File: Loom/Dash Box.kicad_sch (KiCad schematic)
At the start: 28 parts, among them J10 VCU CAN, J11 VCU INPUTS, J12 DASH, J13 OUTPUTS, J14 RTDS, J60 Datalogger Connector, J63 CAN, J64 PWR, J65 MCU_DIN, J66 Segment Display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

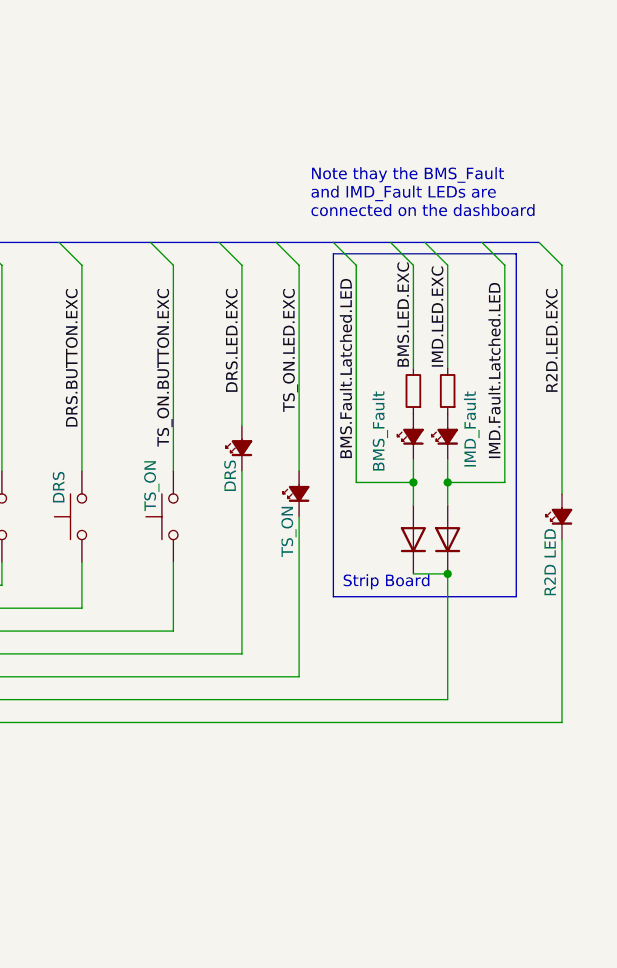
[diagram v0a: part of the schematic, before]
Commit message: fix(Loom): made requested changes + chores
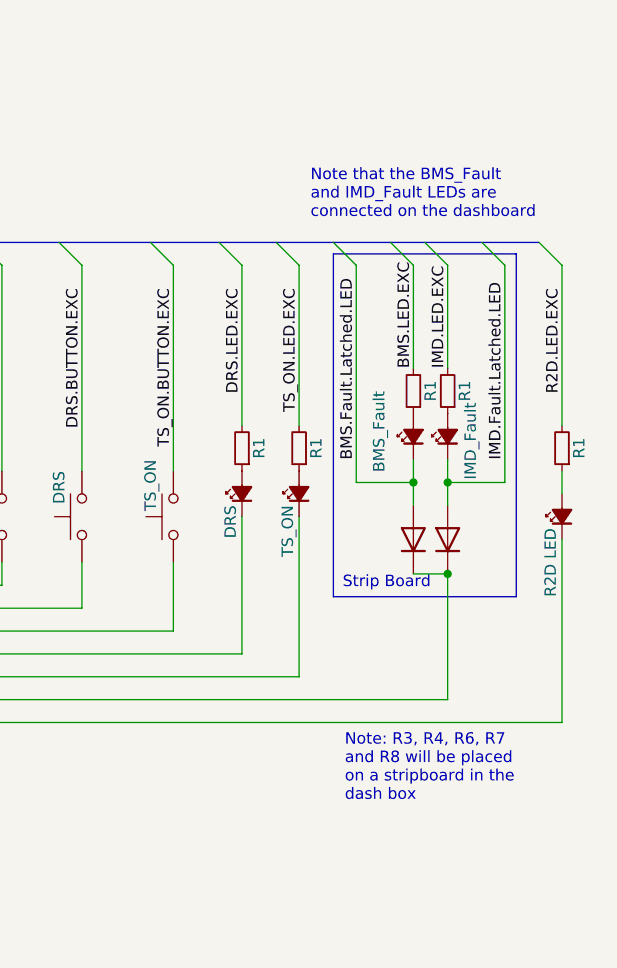
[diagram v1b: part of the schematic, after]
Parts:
- added R1 (x3): R_Small, symbol Device:R_Small
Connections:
- net BMS.LED.EXC: now also R1.2, R1.2, R1.2; no longer D1.2 (A), D2.2 (A), D4.2 (A)
- new net: D4.2 (A), R1.1
- new net: D1.2 (A), R1.1
- new net: D2.2 (A), R1.1
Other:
- note added: "Note that the BMS_Fault and IMD_Fault LEDs are connected on the dashboard"
- note added: "Note: R3, R4, R6, R7 and R8 will be placed on a stripboard in the dash box"
- note removed: "Note thay the BMS_Fault and IMD_Fault LEDs are connected on the dashboard"
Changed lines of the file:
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@@
     (stroke (width 0) (type default))
   )
-  (wire (pts (xy 246.38 68.58) (xy 246.38 88.9))
+  (wire (pts (xy 246.38 73.66) (xy 246.38 88.9))
     (stroke (width 0) (type default))
   )
@@
     (stroke (width 0) (type default))
   )
-  (wire (pts (xy 252.73 45.72) (xy 252.73 68.58))
+  (wire (pts (xy 252.73 45.72) (xy 252.73 63.5))
     (stroke (width 0) (type default))
   )
@@
     (stroke (width 0) (type default))
   )
+  (wire (pts (xy 281.94 68.58) (xy 281.94 71.12))
+    (stroke (width 0) (type default))
+  )
   (wire (pts (xy 78.74 63.5) (xy 101.6 63.5))
     (stroke (width 0) (type default))
@@
     (stroke (width 0) (type default))
   )
-  (wire (pts (xy 281.94 45.72) (xy 281.94 71.12))
+  (wire (pts (xy 281.94 45.72) (xy 281.94 63.5))
     (stroke (width 0) (type default))
   )
@@
     (effects (font (size 1.27 1.27) (color 72 72 72 1)) (justify top))
   )
-  (text "Note thay the BMS_Fault \nand IMD_Fault LEDs are \nconnected on the dashboard"
+  (text "Note: R3, R4, R6, R7\nand R8 will be placed\non a stripboard in the\ndash box"
+    (at 257.81 105.41 0)
+    (effects (font (size 1.27 1.27) (color 255 0 255 1)) (justify left bottom))
+  )
+  (text "Note that the BMS_Fault \nand IMD_Fault LEDs are \nconnected on the dashboard"
     (at 254 40.64 0)
     (effects (font (size 1.27 1.27) (color 255 0 255 1)) (justify left bottom))
@@
     (effects (font (size 1.27 1.27)) (justify left bottom))
   )
-  (label "IMD.LED.EXC" (at 101.6 63.5 180)
-    (effects (font (size 1.27 1.27)) (justify right bottom))
-  )
-  (label "BMS.Fault.Latched.LED" (at 259.08 67.31 90)
+  (label "IMD.LED.EXC" (at 101.6 63.5 180) (fields_autoplaced)
+    (effects (font (size 1.27 1.27)) (justify right bottom))
+  )
+  (label "BMS.Fault.Latched.LED" (at 259.08 67.31 90) (fields_autoplaced)
     (effects (font (size 1.27 1.27)) (justify left bottom))
   )
@@
     (effects (font (size 1.27 1.27)) (justify left bottom))
   )
-  (label "WSS.SIG" (at 139.7 25.4 270)
+  (label "WSS.SIG" (at 139.7 25.4 270) (fields_autoplaced)
     (effects (font (size 1.27 1.27)) (justify right bottom))
   )
@@
     (effects (font (size 1.27 1.27)) (justify left bottom))
   )
-  (label "BMS.LED.EXC" (at 265.43 57.15 90)
+  (label "BMS.LED.EXC" (at 265.43 57.15 90) (fields_autoplaced)
     (effects (font (size 1.27 1.27)) (justify left bottom))
   )
@@
     (effects (font (size 1.27 1.27)) (justify left bottom))
   )
-  (label "TS.READY" (at 147.32 121.92 180)
+  (label "TS.READY" (at 147.32 121.92 180) (fields_autoplaced)
     (effects (font (size 1.27 1.27)) (justify right bottom))
   )
@@
     (effects (font (size 1.27 1.27)) (justify left bottom))
   )
-  (label "TELEM.GPS_ANTENNA" (at 24.13 121.92 0)
+  (label "TELEM.GPS_ANTENNA" (at 24.13 121.92 0) (fields_autoplaced)
     (effects (font (size 1.27 1.27)) (justify left bottom))
   )
@@
     (effects (font (size 1.27 1.27)) (justify left bottom))
   )
-  (label "TELEM.XBEE_ANTENNA" (at 24.13 119.38 0)
+  (label "TELEM.XBEE_ANTENNA" (at 24.13 119.38 0) (fields_autoplaced)
     (effects (font (size 1.27 1.27)) (justify left bottom))
   )
@@
     (effects (font (size 1.27 1.27)) (justify left bottom))
   )
-  (label "BMS.LED.EXC" (at 101.6 66.04 180)
+  (label "BMS.LED.EXC" (at 101.6 66.04 180) (fields_autoplaced)
     (effects (font (size 1.27 1.27)) (justify right bottom))
   )
@@
     (effects (font (size 1.27 1.27)) (justify left bottom))
   )
-  (label "TELEM.XBEE_ANTENNA" (at 90.17 185.42 0)
+  (label "TELEM.XBEE_ANTENNA" (at 90.17 185.42 0) (fields_autoplaced)
     (effects (font (size 1.27 1.27)) (justify left bottom))
   )
@@
     (effects (font (size 1.27 1.27)) (justify left bottom))
   )
-  (label "IMD.Fault.Latched.LED" (at 275.59 67.31 90)
+  (label "IMD.Fault.Latched.LED" (at 275.59 67.31 90) (fields_autoplaced)
     (effects (font (size 1.27 1.27)) (justify left bottom))
   )
@@
     (effects (font (size 1.27 1.27)) (justify left bottom))
   )
-  (label "IMD.LED.EXC" (at 269.24 57.15 90)
+  (label "IMD.LED.EXC" (at 269.24 57.15 90) (fields_autoplaced)
     (effects (font (size 1.27 1.27)) (justify left bottom))
   )
@@
     )
   )
+  (symbol (lib_id "Device:R_Small") (at 281.94 66.04 180) (unit 1)
+    (in_bom yes) (on_board yes) (dnp no)
+    (property "Reference" "R1" (at 283.845 66.04 90)
+      (effects (font (size 1.27 1.27)))
+    )
+    (property "Value" "R_Small" (at 285.75 66.04 90)
+      (effects (font (size 1.27 1.27)) hide)
+    )
+    (property "Footprint" "" (at 281.94 66.04 0)
+      (effects (font (size 1.27 1.27)) hide)
+    )
+    (property "Datasheet" "~" (at 281.94 66.04 0)
+      (effects (font (size 1.27 1.27)) hide)
+    )
+    (pin "1")
+    (pin "2")
+    (instances
+      (project "Loom"
+        (path "/9bc0180a-66dd-482f-994e-fb7ab149eee4/3788bcfb-20fe-4c2f-92ea-25430b35ebcf"
+          (reference "R1") (unit 1)
+        )
+        (path "/9bc0180a-66dd-482f-994e-fb7ab149eee4/466b08e5-662b-404d-99e1-0ba0768d9a56"
+          (reference "R7") (unit 1)
+        )
+      )
+      (project "wiring"
+        (path "/f547916b-3685-4744-bd42-c865a94e86ea/e543dde5-53c9-49c7-95ea-db245558f0fb"
+          (reference "R1") (unit 1)
+        )
+      )
+    )
+  )
   (symbol (lib_id "Connector:Conn_01x01_Pin") (at 85.09 185.42 0) (unit 1)
     (in_bom yes) (on_board yes) (dnp no)
@@
     )
   )
-  (symbol (lib_id "Device:LED_Small_Filled") (at 246.38 66.04 90) (unit 1)
-    (in_bom yes) (on_board yes) (dnp no)
-    (property "Reference" "D1" (at 248.92 65.3415 0)
+  (symbol (lib_id "Device:LED_Small_Filled") (at 246.38 71.12 90) (unit 1)
+    (in_bom yes) (on_board yes) (dnp no)
+    (property "Reference" "D1" (at 248.92 70.4215 0)
       (effects (font (size 1.27 1.27)) (justify right) hide)
     )
-    (property "Value" "DRS" (at 245.11 67.31 0)
+    (property "Value" "DRS" (at 245.11 72.39 0)
       (effects (font (size 1.27 1.27)) (justify right))
     )
-    (property "Footprint" "" (at 246.38 66.04 90)
-      (effects (font (size 1.27 1.27)) hide)
-    )
-    (property "Datasheet" "~" (at 246.38 66.04 90)
+    (property "Footprint" "" (at 246.38 71.12 90)
+      (effects (font (size 1.27 1.27)) hide)
+    )
+    (property "Datasheet" "~" (at 246.38 71.12 90)
       (effects (font (size 1.27 1.27)) hide)
     )
@@
     (in_bom yes) (on_board yes) (dnp no)
     (property "Reference" "R1" (at 267.335 59.69 90)
-      (effects (font (size 1.27 1.27)) hide)
+      (effects (font (size 1.27 1.27)))
     )
     (property "Value" "R_Small" (at 269.24 59.69 90)
@@
       (effects (font (size 1.27 1.27)) (justify right) hide)
     )
-    (property "Value" "IMD_Fault" (at 271.78 59.69 0)
+    (property "Value" "IMD_Fault" (at 271.78 60.96 0)
       (effects (font (size 1.27 1.27)) (justify right))
     )
@@
     (in_bom yes) (on_board yes) (dnp no)
     (property "Reference" "R1" (at 271.145 59.69 90)
-      (effects (font (size 1.27 1.27)) hide)
+      (effects (font (size 1.27 1.27)))
     )
     (property "Value" "R_Small" (at 273.05 59.69 90)
@@
     )
   )
+  (symbol (lib_id "Device:R_Small") (at 246.38 66.04 180) (unit 1)
+    (in_bom yes) (on_board yes) (dnp no)
+    (property "Reference" "R1" (at 248.285 66.04 90)
+      (effects (font (size 1.27 1.27)))
+    )
+    (property "Value" "R_Small" (at 250.19 66.04 90)
+      (effects (font (size 1.27 1.27)) hide)
+    )
+    (property "Footprint" "" (at 246.38 66.04 0)
+      (effects (font (size 1.27 1.27)) hide)
+    )
+    (property "Datasheet" "~" (at 246.38 66.04 0)
+      (effects (font (size 1.27 1.27)) hide)
+    )
+    (pin "1")
+    (pin "2")
+    (instances
+      (project "Loom"
+        (path "/9bc0180a-66dd-482f-994e-fb7ab149eee4/3788bcfb-20fe-4c2f-92ea-25430b35ebcf"
+          (reference "R1") (unit 1)
+        )
+        (path "/9bc0180a-66dd-482f-994e-fb7ab149eee4/466b08e5-662b-404d-99e1-0ba0768d9a56"
+          (reference "R8") (unit 1)
+        )
+      )
+      (project "wiring"
+        (path "/f547916b-3685-4744-bd42-c865a94e86ea/e543dde5-53c9-49c7-95ea-db245558f0fb"
+          (reference "R1") (unit 1)
+        )
+      )
+    )
+  )
   (symbol (lib_id "Switch:SW_Push") (at 219.71 73.66 90) (unit 1)
     (in_bom yes) (on_board yes) (dnp no)
@@
         )
       )
+    )
+  )
+  (symbol (lib_id "Device:R_Small") (at 252.73 66.04 180) (unit 1)
+    (in_bom yes) (on_board yes) (dnp no)
+    (property "Reference" "R1" (at 254.635 66.04 90)
+      (effects (font (size 1.27 1.27)))
+    )
+    (property "Value" "R_Small" (at 256.54 66.04 90)
+      (effects (font (size 1.27 1.27)) hide)
+    )
+    (property "Footprint" "" (at 252.73 66.04 0)
+      (effects (font (size 1.27 1.27)) hide)
+    )
+    (property "Datasheet" "~" (at 252.73 66.04 0)
+      (effects (font (size 1.27 1.27)) hide)
+    )
+    (pin "1")
+    (pin "2")
+    (instances
+      (project "Loom"
+        (path "/9bc0180a-66dd-482f-994e-fb7ab149eee4/3788bcfb-20fe-4c2f-92ea-25430b35ebcf"
+          (reference "R1") (unit 1)
+        )
+        (path "/9bc0180a-66dd-482f-994e-fb7ab149eee4/466b08e5-662b-404d-99e1-0ba0768d9a56"
+          (reference "R6") (unit 1)
+        )
+      )
+      (project "wiring"
+        (path "/f547916b-3685-4744-bd42-c865a94e86ea/e543dde5-53c9-49c7-95ea-db245558f0fb"
+          (reference "R1") (unit 1)
+        )
+      )

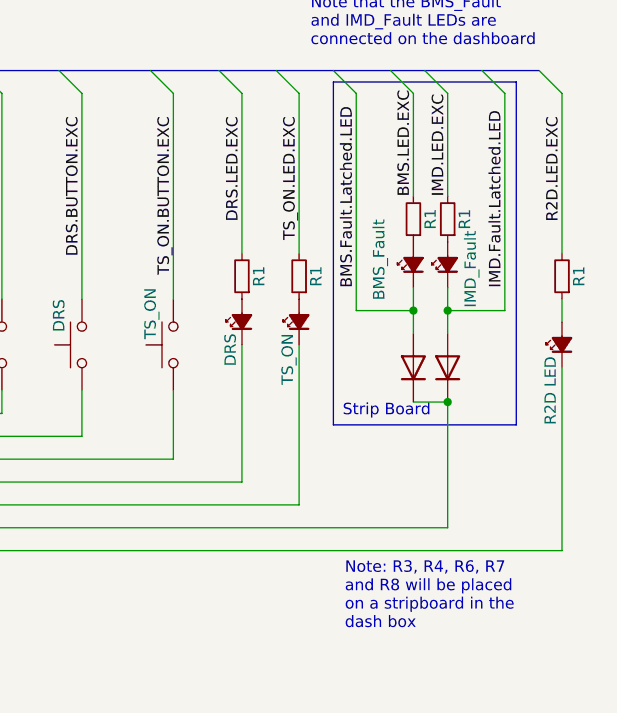
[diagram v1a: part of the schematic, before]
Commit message: fix(Loom): changed position of components
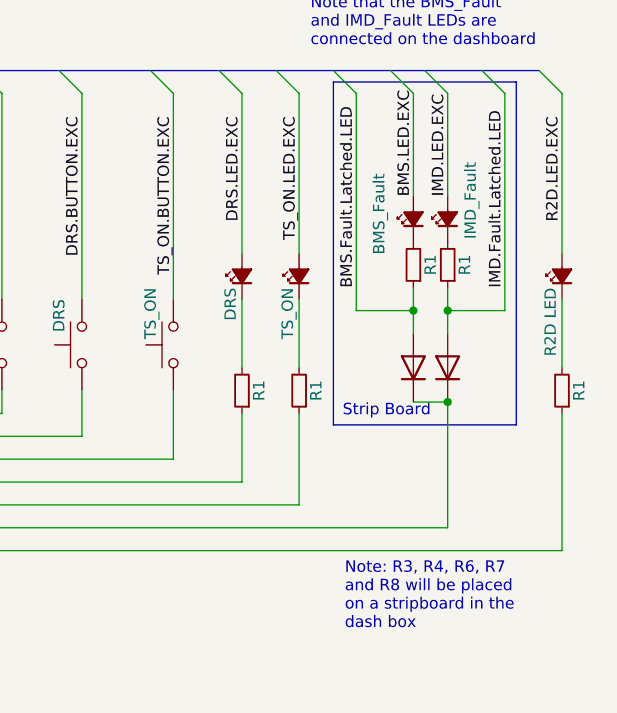
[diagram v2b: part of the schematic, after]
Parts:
- removed R1 (x5): R_Small, symbol Device:R_Small
- added R1 (x5): R_Small, symbol Device:R_Small
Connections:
- net BMS.Fault.Latched.LED: now also R1.1; no longer D3.1 (K)
- net BMS.LED.EXC: now also D1.2 (A), D2.2 (A), D3.2 (A), D4.2 (A), D5.2 (A)
- net DRS_LED: now also R1.1; no longer D1.1 (K)
- net IMD.Fault.Latched.LED: now also R1.1; no longer D5.1 (K)
- net R2D_LED: now also R1.1; no longer D4.1 (K)
- net TS_ON_LED: now also R1.1; no longer D2.1 (K)
- new net: D2.1 (K), R1.2
- new net: D4.1 (K), R1.2
- new net: D1.1 (K), R1.2
- new net: D3.1 (K), R1.2
- new net: D5.1 (K), R1.2

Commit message: feat(loom): minor tweaks to dash + VCU connections
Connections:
- net VCU.VC_LEDS: now reaches D6.1 (K), D7.1 (K), J12.7 (Pin_7)
- net DRS_BTN renamed VCU.DRS_BTN
- net DRS_LED renamed VCU.DRS_LED
- net R2D_BTN renamed VCU.R2D_BTN
- net R2D_LED renamed VCU.R2D_LED
- net TS_ON_BTN renamed VCU.TS_ON_BTN
- net TS_ON_LED renamed VCU.TS_ON_LED
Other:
- note added: "Note: R3, R4, R6, R7 and R8 will be placed on a small PCB in the dash box"
- note removed: "Note: R3, R4, R6, R7 and R8 will be placed on a stripboard in the dash box"
- moved on the sheet: R1
